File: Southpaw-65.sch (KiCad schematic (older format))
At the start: 214 parts, among them J1 USB_C_Receptacle_USB2.0, SW1 SW_Push, SW2 Rotary_Encoder, SW3 Rotary_Encoder, U1 ATmega32A-PU, Y1 16MHz

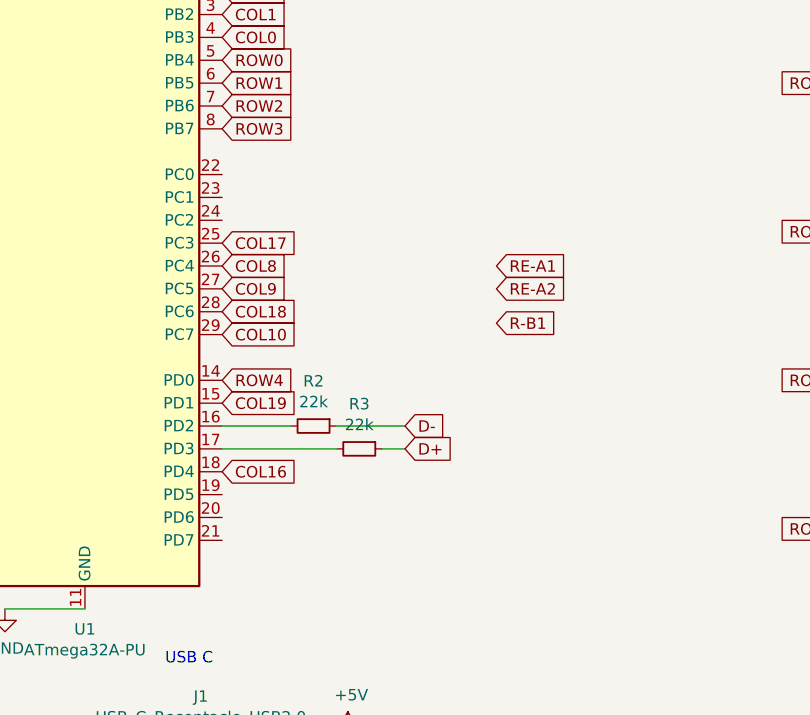
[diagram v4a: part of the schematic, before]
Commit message: Finished encoders and worked on fills
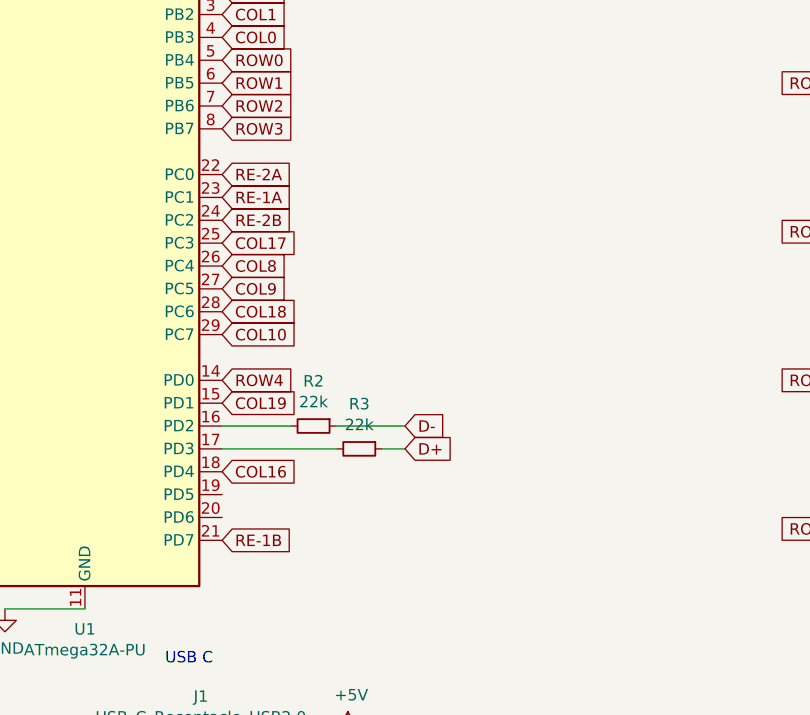
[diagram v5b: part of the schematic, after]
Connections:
- net RE-1A: now also U1.23 (PC1)
- net RE-1B: now also U1.21 (PD7)
- net RE-2A: now also U1.22 (PC0)
- net RE-2B: now also U1.24 (PC2)
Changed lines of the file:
@@
 Text Notes 5250 5000 0    50   ~ 0
 Reset
-Text GLabel 3200 3250 2    50   Input ~ 0
-RE-A1
-Text GLabel 3200 3500 2    50   Input ~ 0
-R-B1
+Text GLabel 2000 2950 2    50   Input ~ 0
+RE-1A
+Text GLabel 2000 4450 2    50   Input ~ 0
+RE-1B
 Wire Wire Line
 	16800 2050 16800 2700
@@
 Text GLabel 2000 3450 2    50   Input ~ 0
 COL18
-Text GLabel 3200 3350 2    50   Input ~ 0
-RE-A2
+Text GLabel 2000 2850 2    50   Input ~ 0
+RE-2A
+Text GLabel 2000 3050 2    50   Input ~ 0
+RE-2B
 $EndSCHEMATC

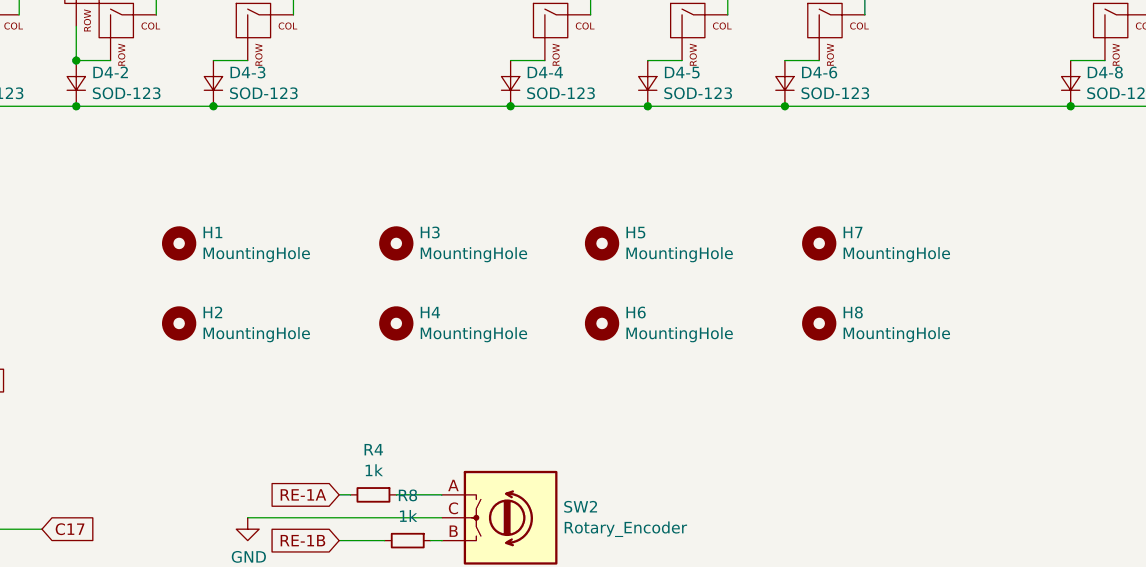
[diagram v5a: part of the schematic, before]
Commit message: Altered bottom row layout and equalized dimensions of board
Left and right side of board were of different distances from the switches, so they were fixed to be equal. Bottom Row layout is now 1.25/12.5/1.25 rather than 1.5/1/1.25 this does not change the total layout as it is redistribution of space between the three keys.
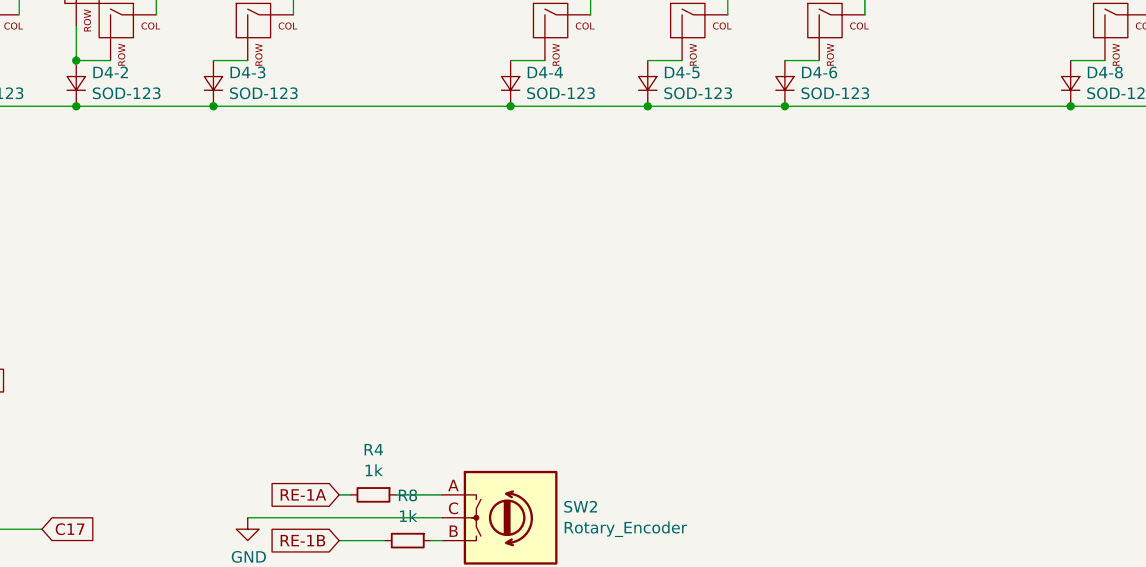
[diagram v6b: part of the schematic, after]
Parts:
- removed H1, H2, H3, H4, H5, H6, H7, H8: MountingHole, MountingHole:MountingHole_3.2mm_M3, symbol Mechanical:MountingHole
- MX4-4: footprint MX_Only:MXOnly-1.5U -> MX_Only:MXOnly-1.25U
- MX4-5: footprint MX_Only:MXOnly-1U -> MX_Only:MXOnly-1.25U
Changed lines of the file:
@@
 F 0 "MX4-4" H 8233 4273 60  0000 C CNN
 F 1 "MX-NoLED" H 8233 4199 20  0000 C CNN
-F 2 "MX_Only:MXOnly-1.5U" H 7575 4025 60  0001 C CNN
+F 2 "MX_Only:MXOnly-1.25U" H 7575 4025 60  0001 C CNN
 F 3 "" H 7575 4025 60  0001 C CNN
 	1    8200 4050
@@
 F 0 "MX4-5" H 8833 4273 60  0000 C CNN
 F 1 "MX-NoLED" H 8833 4199 20  0000 C CNN
-F 2 "MX_Only:MXOnly-1U" H 8175 4025 60  0001 C CNN
+F 2 "MX_Only:MXOnly-1.25U" H 8175 4025 60  0001 C CNN
 F 3 "" H 8175 4025 60  0001 C CNN
 	1    8800 4050
@@
 Connection ~ 16800 2050
 $Comp
-L Mechanical:MountingHole H1
-U 1 1 5F9978E5
-P 6550 5000
-F 0 "H1" H 6650 5046 50  0000 L CNN
-F 1 "MountingHole" H 6650 4955 50  0000 L CNN
-F 2 "MountingHole:MountingHole_3.2mm_M3" H 6550 5000 50  0001 C CNN
-F 3 "~" H 6550 5000 50  0001 C CNN
-	1    6550 5000
-	1    0    0    -1
-$EndComp
-$Comp
-L Mechanical:MountingHole H2
-U 1 1 5F999F3C
-P 6550 5350
-F 0 "H2" H 6650 5396 50  0000 L CNN
-F 1 "MountingHole" H 6650 5305 50  0000 L CNN
-F 2 "MountingHole:MountingHole_3.2mm_M3" H 6550 5350 50  0001 C CNN
-F 3 "~" H 6550 5350 50  0001 C CNN
-	1    6550 5350
-	1    0    0    -1
-$EndComp
-$Comp
-L Mechanical:MountingHole H3
-U 1 1 5F9B455A
-P 7500 5000
-F 0 "H3" H 7600 5046 50  0000 L CNN
-F 1 "MountingHole" H 7600 4955 50  0000 L CNN
-F 2 "MountingHole:MountingHole_3.2mm_M3" H 7500 5000 50  0001 C CNN
-F 3 "~" H 7500 5000 50  0001 C CNN
-	1    7500 5000
-	1    0    0    -1
-$EndComp
-$Comp
-L Mechanical:MountingHole H4
-U 1 1 5F9B4564
-P 7500 5350
-F 0 "H4" H 7600 5396 50  0000 L CNN
-F 1 "MountingHole" H 7600 5305 50  0000 L CNN
-F 2 "MountingHole:MountingHole_3.2mm_M3" H 7500 5350 50  0001 C CNN
-F 3 "~" H 7500 5350 50  0001 C CNN
-	1    7500 5350
-	1    0    0    -1
-$EndComp
-$Comp
-L Mechanical:MountingHole H5
-U 1 1 5F9CEEB3
-P 8400 5000
-F 0 "H5" H 8500 5046 50  0000 L CNN
-F 1 "MountingHole" H 8500 4955 50  0000 L CNN
-F 2 "MountingHole:MountingHole_3.2mm_M3" H 8400 5000 50  0001 C CNN
-F 3 "~" H 8400 5000 50  0001 C CNN
-	1    8400 5000
-	1    0    0    -1
-$EndComp
-$Comp
-L Mechanical:MountingHole H6
-U 1 1 5F9CEEBD
-P 8400 5350
-F 0 "H6" H 8500 5396 50  0000 L CNN
-F 1 "MountingHole" H 8500 5305 50  0000 L CNN
-F 2 "MountingHole:MountingHole_3.2mm_M3" H 8400 5350 50  0001 C CNN
-F 3 "~" H 8400 5350 50  0001 C CNN
-	1    8400 5350
-	1    0    0    -1
-$EndComp
-$Comp
-L Mechanical:MountingHole H7
-U 1 1 5F9CEEC7
-P 9350 5000
-F 0 "H7" H 9450 5046 50  0000 L CNN
-F 1 "MountingHole" H 9450 4955 50  0000 L CNN
-F 2 "MountingHole:MountingHole_3.2mm_M3" H 9350 5000 50  0001 C CNN
-F 3 "~" H 9350 5000 50  0001 C CNN
-	1    9350 5000
-	1    0    0    -1
-$EndComp
-$Comp
-L Mechanical:MountingHole H8
-U 1 1 5F9CEED1
-P 9350 5350
-F 0 "H8" H 9450 5396 50  0000 L CNN
-F 1 "MountingHole" H 9450 5305 50  0000 L CNN
-F 2 "MountingHole:MountingHole_3.2mm_M3" H 9350 5350 50  0001 C CNN
-F 3 "~" H 9350 5350 50  0001 C CNN
-	1    9350 5350
-	1    0    0    -1
-$EndComp
-$Comp
 L MX_Alps_Hybrid:MX-NoLED MX0-17B1

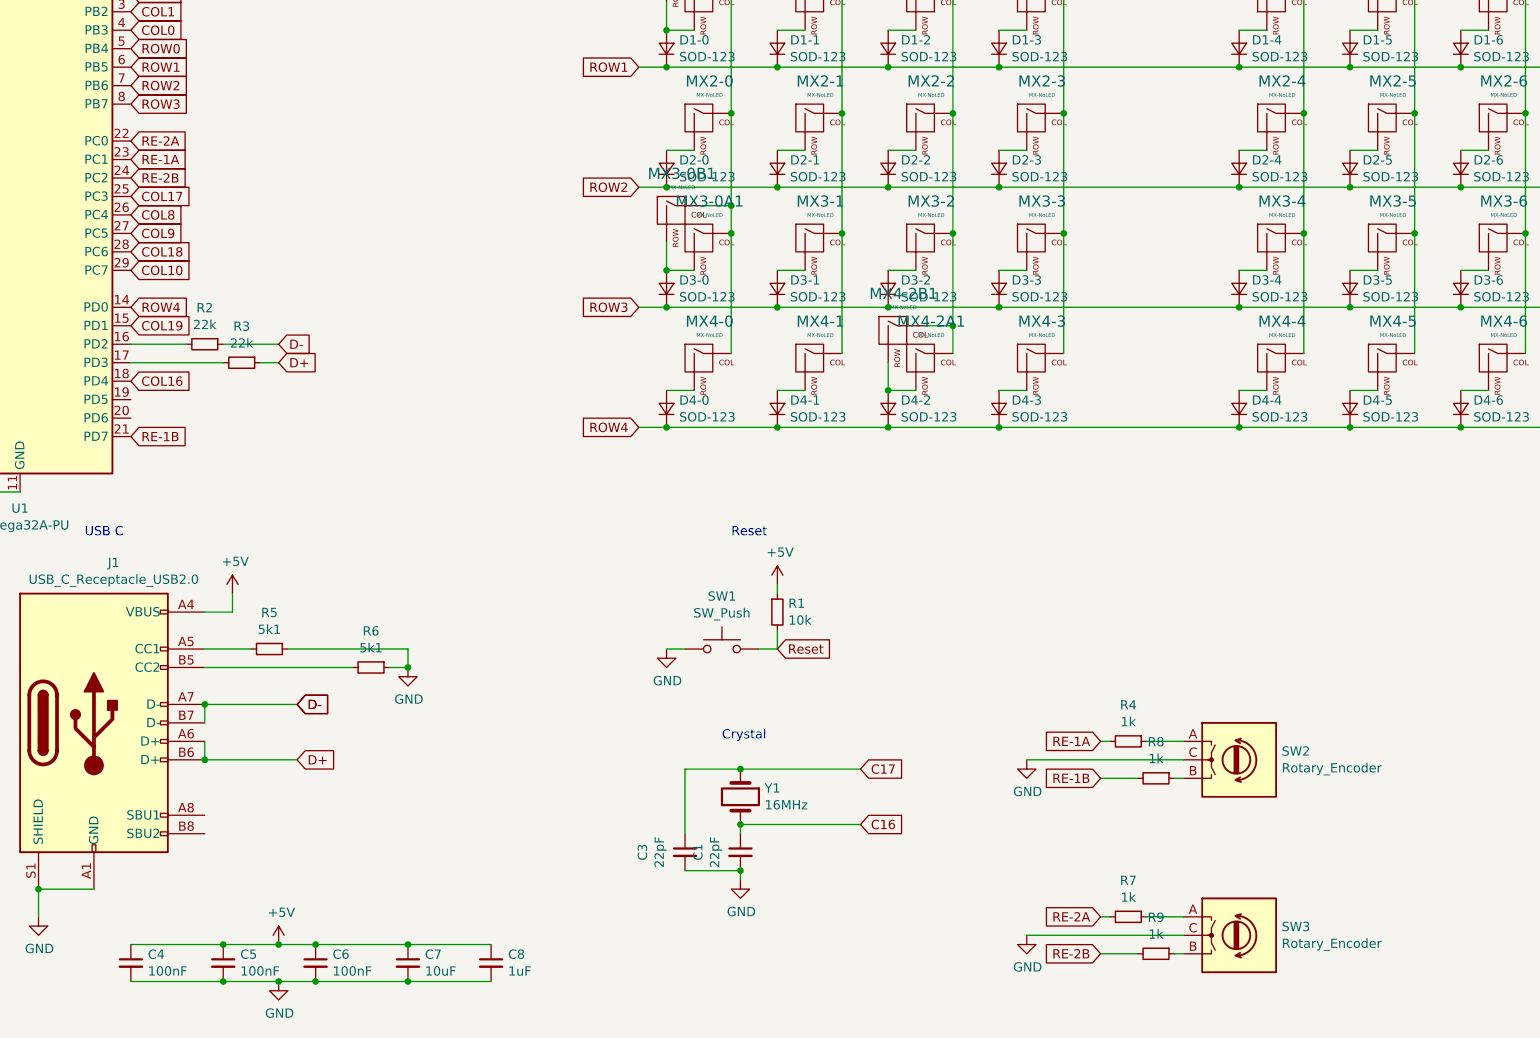
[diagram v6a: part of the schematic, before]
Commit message: Switched the side which the USB is supposed to lie on
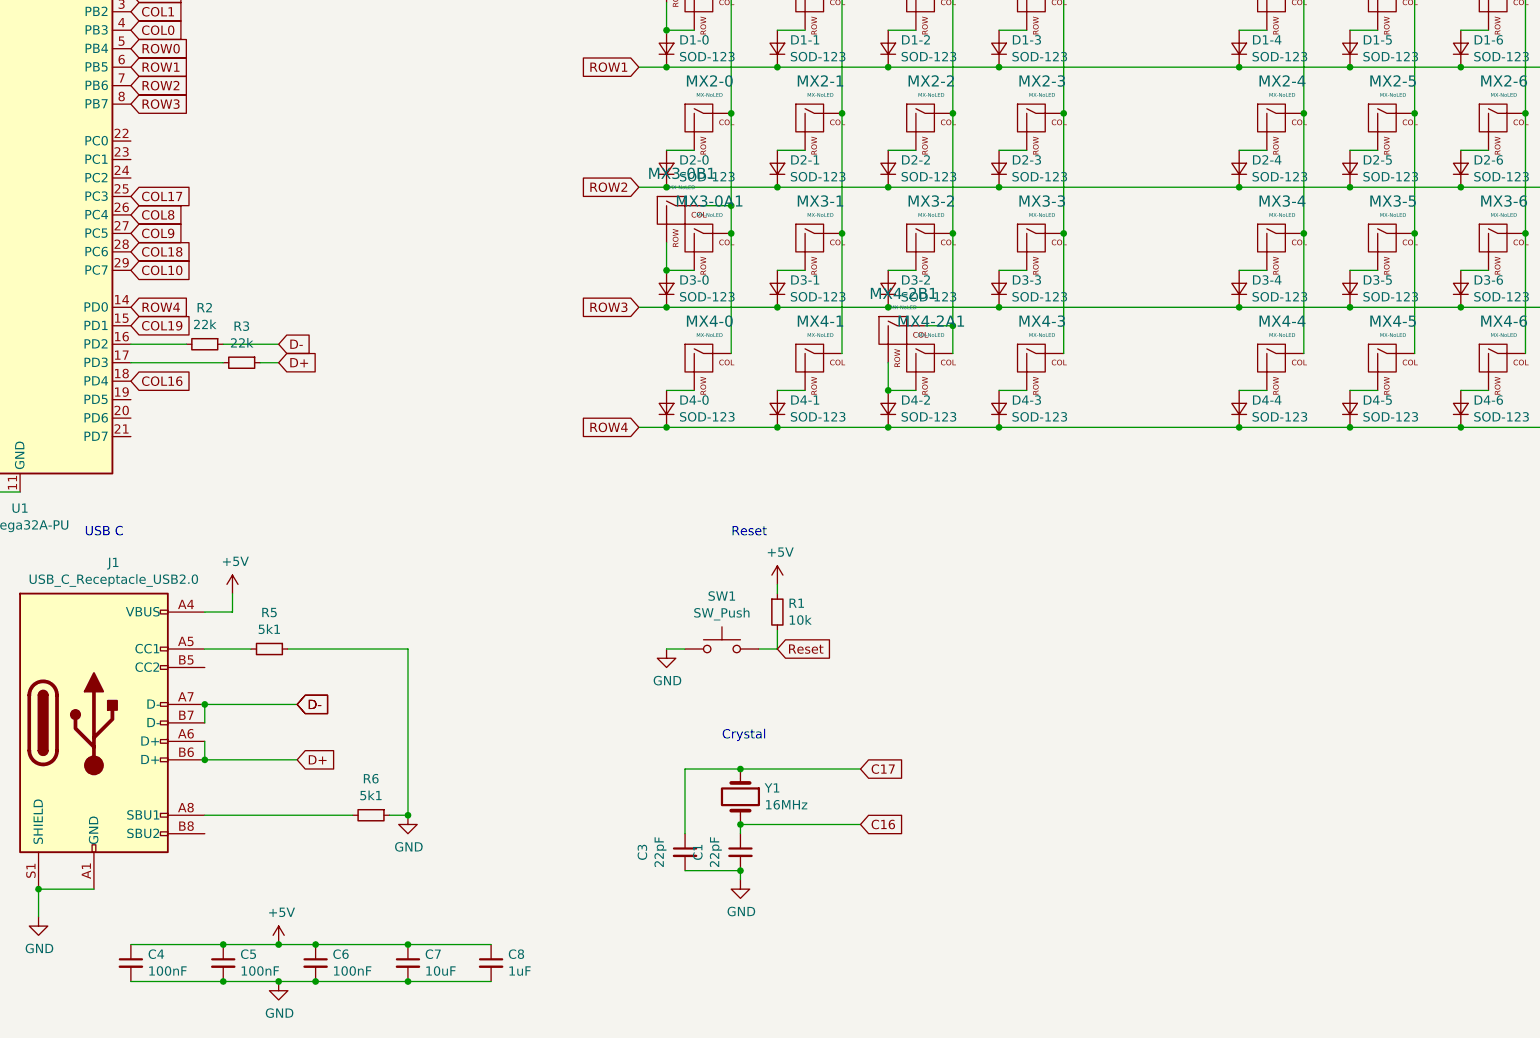
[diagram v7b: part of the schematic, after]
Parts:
- removed R4, R7, R8, R9: 1k, Resistor_THT:R_Axial_DIN0207_L6.3mm_D2.5mm_P7.62mm_Horizontal, symbol Device:R_Small
- removed SW2, SW3: Rotary_Encoder, Rotary_Encoder:RotaryEncoder_Alps_EC11E_Vertical_H20mm, symbol Device:Rotary_Encoder
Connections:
- net at J1.A8 (SBU1): now also R6.2
- net at J1.B5 (CC2): no longer R6.2
- net RE-1A: no longer names the net of U1.23 (PC1)
- net RE-1B: no longer names the net of U1.21 (PD7)
- net RE-2A: no longer names the net of U1.22 (PC0)
- net RE-2B: no longer names the net of U1.24 (PC2)
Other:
- moved on the sheet: R6
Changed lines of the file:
@@
 L Device:R_Small R6
 U 1 1 5F8CAC0E
-P 3300 5700
-F 0 "R6" V 3104 5700 50  0000 C CNN
-F 1 "5k1" V 3195 5700 50  0000 C CNN
-F 2 "Resistor_THT:R_Axial_DIN0207_L6.3mm_D2.5mm_P7.62mm_Horizontal" H 3300 5700 50  0001 C CNN
-F 3 "~" H 3300 5700 50  0001 C CNN
-	1    3300 5700
+P 3300 6500
+F 0 "R6" V 3104 6500 50  0000 C CNN
+F 1 "5k1" V 3195 6500 50  0000 C CNN
+F 2 "Resistor_THT:R_Axial_DIN0207_L6.3mm_D2.5mm_P7.62mm_Horizontal" H 3300 6500 50  0001 C CNN
+F 3 "~" H 3300 6500 50  0001 C CNN
+	1    3300 6500
 	0    1    1    0
 $EndComp
@@
 	2400 5600 2650 5600
 Wire Wire Line
-	2400 5700 3200 5700
+	2400 6500 3200 6500
 $Comp
 L Device:C_Small C8
@@
 L power:GND #PWR0108
 U 1 1 5F8DAB62
-P 3500 5700
-F 0 "#PWR0108" H 3500 5450 50  0001 C CNN
-F 1 "GND" H 3505 5527 50  0000 C CNN
-F 2 "" H 3500 5700 50  0001 C CNN
-F 3 "" H 3500 5700 50  0001 C CNN
-	1    3500 5700
+P 3500 6500
+F 0 "#PWR0108" H 3500 6250 50  0001 C CNN
+F 1 "GND" H 3505 6327 50  0000 C CNN
+F 2 "" H 3500 6500 50  0001 C CNN
+F 3 "" H 3500 6500 50  0001 C CNN
+	1    3500 6500
 	1    0    0    -1
 $EndComp
@@
 	2850 5600 3500 5600
 Wire Wire Line
-	3500 5600 3500 5700
-Wire Wire Line
-	3400 5700 3500 5700
-Connection ~ 3500 5700
+	3400 6500 3500 6500
 $Comp
 L power:+5V #PWR0109
@@
 Text Notes 5250 5000 0    50   ~ 0
 Reset
-Text GLabel 2000 2950 2    50   Input ~ 0
-RE-1A
-Text GLabel 2000 4450 2    50   Input ~ 0
-RE-1B
 Wire Wire Line
 	16800 2050 16800 2700
@@
 Wire Wire Line
 	5250 1900 5250 1400
-$Comp
-L Device:Rotary_Encoder SW2
-U 1 1 5FAEB0EF
-P 8000 6200
-F 0 "SW2" H 8230 6246 50  0000 L CNN
-F 1 "Rotary_Encoder" H 8230 6155 50  0000 L CNN
-F 2 "Rotary_Encoder:RotaryEncoder_Alps_EC11E_Vertical_H20mm" H 7850 6360 50  0001 C CNN
-F 3 "~" H 8000 6460 50  0001 C CNN
-	1    8000 6200
-	1    0    0    -1
-$EndComp
-Text GLabel 7250 6100 0    50   Input ~ 0
-RE-1A
-Text GLabel 7250 6300 0    50   Input ~ 0
-RE-1B
-$Comp
-L Device:R_Small R8
-U 1 1 5FB2C844
-P 7550 6300
-F 0 "R8" V 7354 6300 50  0000 C CNN
-F 1 "1k" V 7445 6300 50  0000 C CNN
-F 2 "Resistor_THT:R_Axial_DIN0207_L6.3mm_D2.5mm_P7.62mm_Horizontal" H 7550 6300 50  0001 C CNN
-F 3 "~" H 7550 6300 50  0001 C CNN
-	1    7550 6300
-	0    1    1    0
-$EndComp
-$Comp
-L Device:R_Small R4
-U 1 1 5FB2CE4E
-P 7400 6100
-F 0 "R4" V 7204 6100 50  0000 C CNN
-F 1 "1k" V 7295 6100 50  0000 C CNN
-F 2 "Resistor_THT:R_Axial_DIN0207_L6.3mm_D2.5mm_P7.62mm_Horizontal" H 7400 6100 50  0001 C CNN
-F 3 "~" H 7400 6100 50  0001 C CNN
-	1    7400 6100
-	0    1    1    0
-$EndComp
-Wire Wire Line
-	7700 6100 7500 6100
-Wire Wire Line
-	7250 6300 7450 6300
-Wire Wire Line
-	7650 6300 7700 6300
-Wire Wire Line
-	7300 6100 7250 6100
-$Comp
-L power:GND #PWR0111
-U 1 1 5FBE38D5
-P 6850 6200
-F 0 "#PWR0111" H 6850 5950 50  0001 C CNN
-F 1 "GND" H 6855 6027 50  0000 C CNN
-F 2 "" H 6850 6200 50  0001 C CNN
-F 3 "" H 6850 6200 50  0001 C CNN
-	1    6850 6200
-	1    0    0    -1
-$EndComp
-$Comp
-L Device:Rotary_Encoder SW3
-U 1 1 5FC3F347
-P 8000 7150
-F 0 "SW3" H 8230 7196 50  0000 L CNN
-F 1 "Rotary_Encoder" H 8230 7105 50  0000 L CNN
-F 2 "Rotary_Encoder:RotaryEncoder_Alps_EC11E_Vertical_H20mm" H 7850 7310 50  0001 C CNN
-F 3 "~" H 8000 7410 50  0001 C CNN
-	1    8000 7150
-	1    0    0    -1
-$EndComp
-Text GLabel 7250 7050 0    50   Input ~ 0
-RE-2A
-Text GLabel 7250 7250 0    50   Input ~ 0
-RE-2B
-$Comp
-L Device:R_Small R9
-U 1 1 5FC3F353
-P 7550 7250
-F 0 "R9" V 7354 7250 50  0000 C CNN
-F 1 "1k" V 7445 7250 50  0000 C CNN
-F 2 "Resistor_THT:R_Axial_DIN0207_L6.3mm_D2.5mm_P7.62mm_Horizontal" H 7550 7250 50  0001 C CNN
-F 3 "~" H 7550 7250 50  0001 C CNN
-	1    7550 7250
-	0    1    1    0
-$EndComp
-$Comp
-L Device:R_Small R7
-U 1 1 5FC3F35D
-P 7400 7050
-F 0 "R7" V 7204 7050 50  0000 C CNN
-F 1 "1k" V 7295 7050 50  0000 C CNN
-F 2 "Resistor_THT:R_Axial_DIN0207_L6.3mm_D2.5mm_P7.62mm_Horizontal" H 7400 7050 50  0001 C CNN
-F 3 "~" H 7400 7050 50  0001 C CNN
-	1    7400 7050
-	0    1    1    0
-$EndComp
-Wire Wire Line
-	7700 7050 7500 7050
-Wire Wire Line
-	7250 7250 7450 7250
-Wire Wire Line
-	7650 7250 7700 7250
-Wire Wire Line
-	7300 7050 7250 7050
-$Comp
-L power:GND #PWR0112
-U 1 1 5FC3F36C
-P 6850 7150
-F 0 "#PWR0112" H 6850 6900 50  0001 C CNN
-F 1 "GND" H 6855 6977 50  0000 C CNN
-F 2 "" H 6850 7150 50  0001 C CNN
-F 3 "" H 6850 7150 50  0001 C CNN
-	1    6850 7150
-	1    0    0    -1
-$EndComp
-Wire Wire Line
-	6850 6200 7700 6200
-Wire Wire Line
-	6850 7150 7700 7150
 Text GLabel 2000 3450 2    50   Input ~ 0
 COL18
-Text GLabel 2000 2850 2    50   Input ~ 0
-RE-2A
-Text GLabel 2000 3050 2    50   Input ~ 0
-RE-2B
+Wire Wire Line
+	3500 5600 3500 6500
+Connection ~ 3500 6500
 $EndSCHEMATC
